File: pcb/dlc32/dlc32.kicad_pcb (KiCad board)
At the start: 2 copper layers, 99.8 x 60.2 mm, 58 parts, among them IC1 74HCT08, IC2 74HCT04, J1 DOOR1, J10 VALVE/CHILLER SSR PWR, J11 Conn_01x02, J12 Conn_01x03, J13 Conn_01x03, J14 Conn_02x05_Odd_Even, J15 Conn_01x05, J16 Conn_01x03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

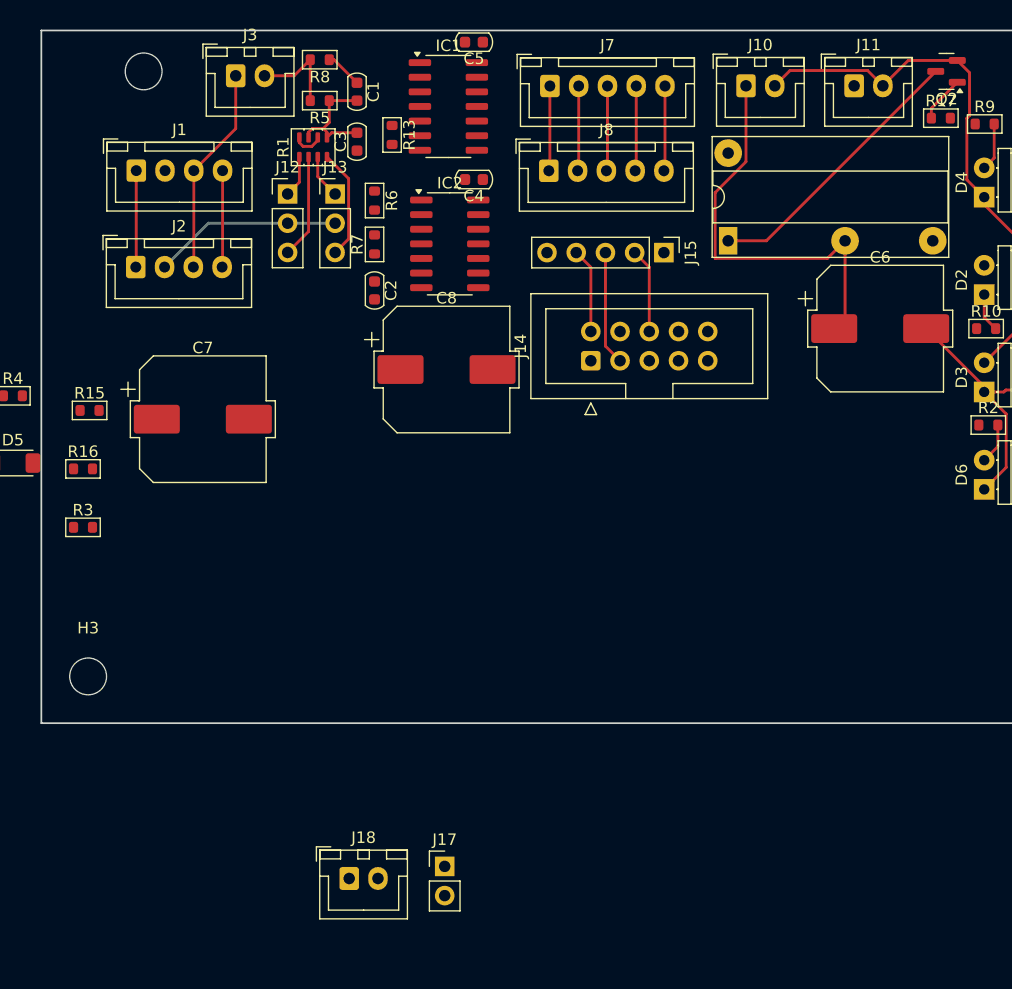
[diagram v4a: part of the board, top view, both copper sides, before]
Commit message: Fix footprint for R1.
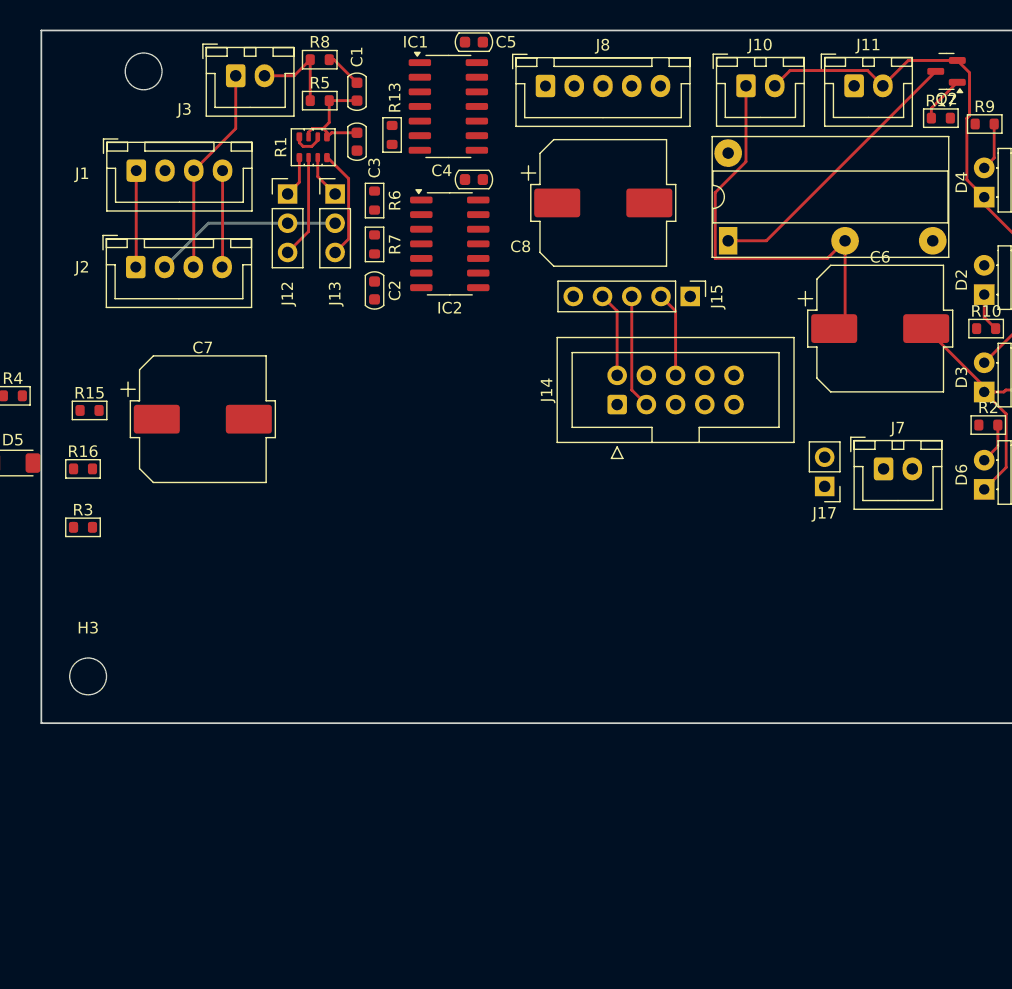
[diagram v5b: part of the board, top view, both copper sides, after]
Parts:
- removed the J7 at (118.1, 29.2)
- J11: value Conn_01x02 -> EXHAUST
- J12: value Conn_01x03 -> DOORJMP1
- J13: value Conn_01x03 -> DOORJMP2
- J14: value Conn_02x05_Odd_Even -> EXT1
- J15: value Conn_01x05 -> COM2
- J16: value Conn_01x03 -> DLC32:J18
- J17: value Conn_01x02 -> EXT PWR
- J7: renamed from J18; value Conn_01x02 -> 5V PWR
- R1: footprint PCM_Resistor_SMD_AKL:R_Array_Concave_4x0603 -> PCM_Resistor_SMD_AKL:R_Array_Convex_4x0603
- moved J7 58.5 mm to (147.1, 62.5)
- moved J17 46.7 mm to (142.0, 64.0), turned to 180 degrees
- moved C8 19.9 mm to (122.7, 39.4)
- moved J8 7.37 mm to (117.7, 29.2)
- moved J14 4.44 mm to (124.0, 56.9)
- moved J15 4.44 mm to (130.3, 47.5)
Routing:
- net GND: track 105.5 -> 98.1 mm
- net +5V: track 28.2 -> 20.8 mm
- net Net-(J8-Pin_4): track 7.40 -> 0.00 mm
- net Net-(J8-Pin_3): track 7.40 -> 0.00 mm
- net Net-(J8-Pin_2): track 7.40 -> 0.00 mm

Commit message: Route some more.
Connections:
- IC1 pad 1: LASER_EN -> Net-(C1-Pad1)
- IC1 pad 11: Net-(IC1-Pad11) -> Net-(J8-Pin_3)
- IC1 pad 12: Net-(C1-Pad1) -> LASER_EN
- IC1 pad 2: Net-(IC1-Pad11) -> Net-(IC1-Pad2)
- IC1 pad 3: Net-(J8-Pin_3) -> Net-(IC1-Pad13)
- IC1 pad 4: Net-(IC1-Pad11) -> Net-(IC1-Pad13)
- IC1 pad 8: Net-(IC1-Pad13) -> Net-(IC1-Pad2)
- IC2 pad 13: Net-(IC1-Pad13) -> Net-(IC1-Pad2)
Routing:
- net +5V: track 20.8 -> 145.2 mm, vias 0 -> 4
- net Net-(J3-Pin_2): track 8.11 -> 93.8 mm
- net Net-(J8-Pin_3): track 0.00 -> 50.7 mm, vias 0 -> 2
- net Net-(IC2-Pad12): track 0.00 -> 47.8 mm, vias 0 -> 2
- net Net-(IC2-Pad10): track 0.00 -> 46.1 mm, vias 0 -> 2
- net GND: track 98.1 -> 141.4 mm
- net FAN: track 0.00 -> 34.5 mm, vias 0 -> 2
- net Net-(J8-Pin_4): track 0.00 -> 20.3 mm, vias 0 -> 1
- net Net-(J1-Pin_2): track 0.00 -> 19.6 mm, vias 0 -> 1
- net Net-(C2-Pad1): track 0.00 -> 19.1 mm, vias 0 -> 2
- net Net-(IC1-Pad2): track 0.00 -> 17.5 mm, vias 0 -> 4
- net Net-(J11-Pin_1): track 0.00 -> 16.3 mm
- net Net-(C3-Pad1): track 0.00 -> 16.0 mm, vias 0 -> 2
- net Net-(IC1-Pad13): track 0.00 -> 6.75 mm
- net Net-(C1-Pad1): track 3.24 -> 9.43 mm
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
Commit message: Route.
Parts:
- added H5: MountingHole, MountingHole:MountingHole_3.2mm_M3, F.Cu at (169.6, 33.2)
- added H6: MountingHole, MountingHole:MountingHole_3.2mm_M3, F.Cu at (169.7, 58.7)
- moved R12 117.5 mm to (109.0, 53.1), turned to 180 degrees
- moved R11 114.2 mm to (109.0, 55.1), turned to 0 degrees
- moved D1 113.4 mm to (111.8, 57.9), turned to 180 degrees
- moved J6 106.4 mm to (113.3, 64.8), turned to 180 degrees
- moved Q1 106.2 mm to (102.5, 55.1), turned to 0 degrees
- moved J4 93.2 mm to (103.6, 64.8), turned to 180 degrees
- moved J5 83.0 mm to (94.5, 64.8), turned to 180 degrees
- moved J9 55.2 mm to (134.4, 62.7)
- moved H4 45.1 mm to (127.5, 64.5)
- moved R4 23.1 mm to (93.9, 50.8), turned to 90 degrees
- moved D5 22.4 mm to (91.4, 51.8), turned to 90 degrees
- moved R3 18.7 mm to (88.4, 52.3), turned to 180 degrees
- moved H3 16.0 mm to (77.5, 64.5)
- moved R16 13.4 mm to (88.9, 55.4), turned to 180 degrees
- moved R15 12.4 mm to (88.4, 50.5)
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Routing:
- net GND: track 141.4 -> 281.0 mm, vias 0 -> 5
- net +V_VALVE: track 44.4 -> 122.7 mm, vias 0 -> 2
- net Net-(D1-A): track 0.00 -> 67.1 mm, vias 0 -> 2
- net LASER_EN: track 0.00 -> 38.2 mm, vias 0 -> 3
- net VALVE_CTRL: track 0.00 -> 33.4 mm
- net Net-(J8-Pin_2): track 0.00 -> 26.9 mm
- net Net-(IC2-Pad9): track 0.00 -> 26.4 mm, vias 0 -> 2
- net FAN: track 34.5 -> 60.2 mm, vias 2 -> 3
- net Net-(D5-K): track 0.00 -> 23.9 mm, vias 0 -> 2
- net Net-(J14-Pin_1): track 0.00 -> 20.3 mm
- net Net-(IC2-Pad6): track 0.00 -> 14.9 mm
- net Net-(J8-Pin_3): track 50.7 -> 62.4 mm
- net Net-(Q1-G): track 0.00 -> 11.0 mm
- net +5V: track 145.2 -> 153.4 mm
- net Net-(J4-Pin_2): track 0.00 -> 6.64 mm
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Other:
- board size 99.8 x 60.2 mm -> 99.8 x 43.9 mm

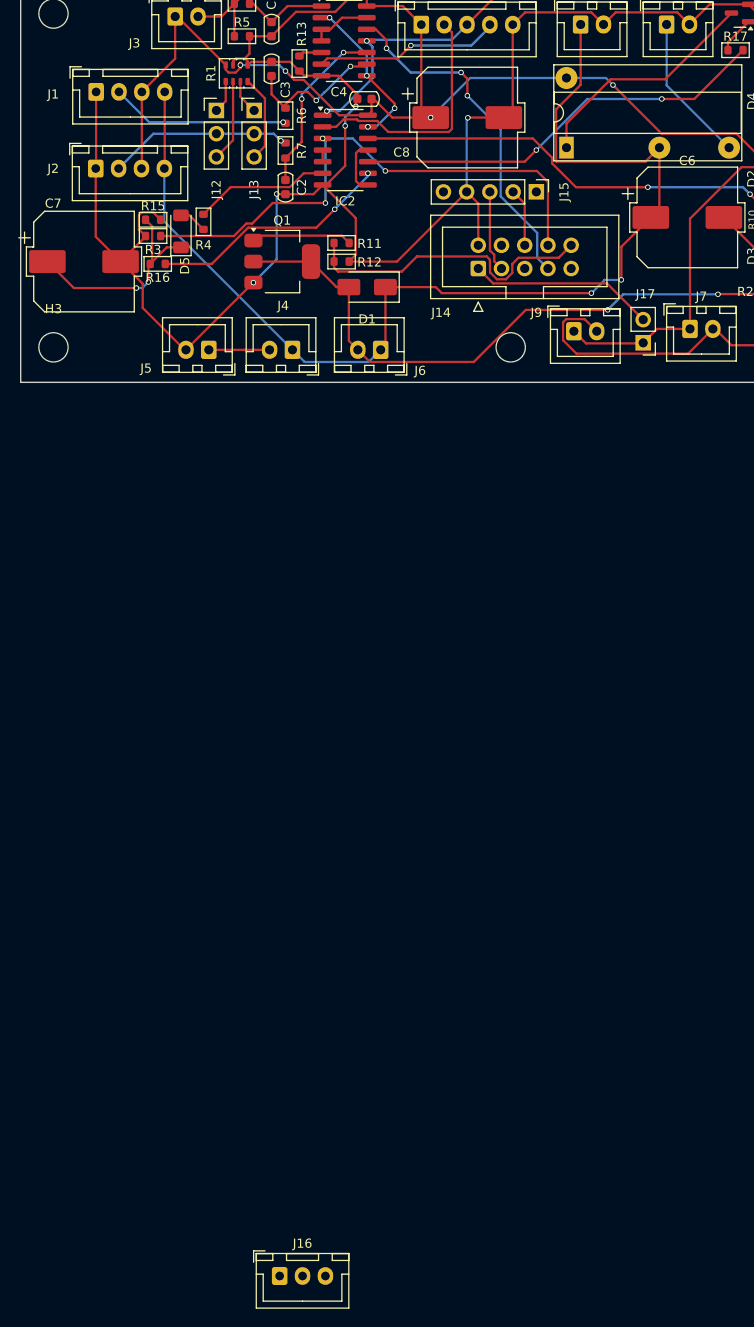
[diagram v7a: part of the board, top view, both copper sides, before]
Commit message: Complete routing.
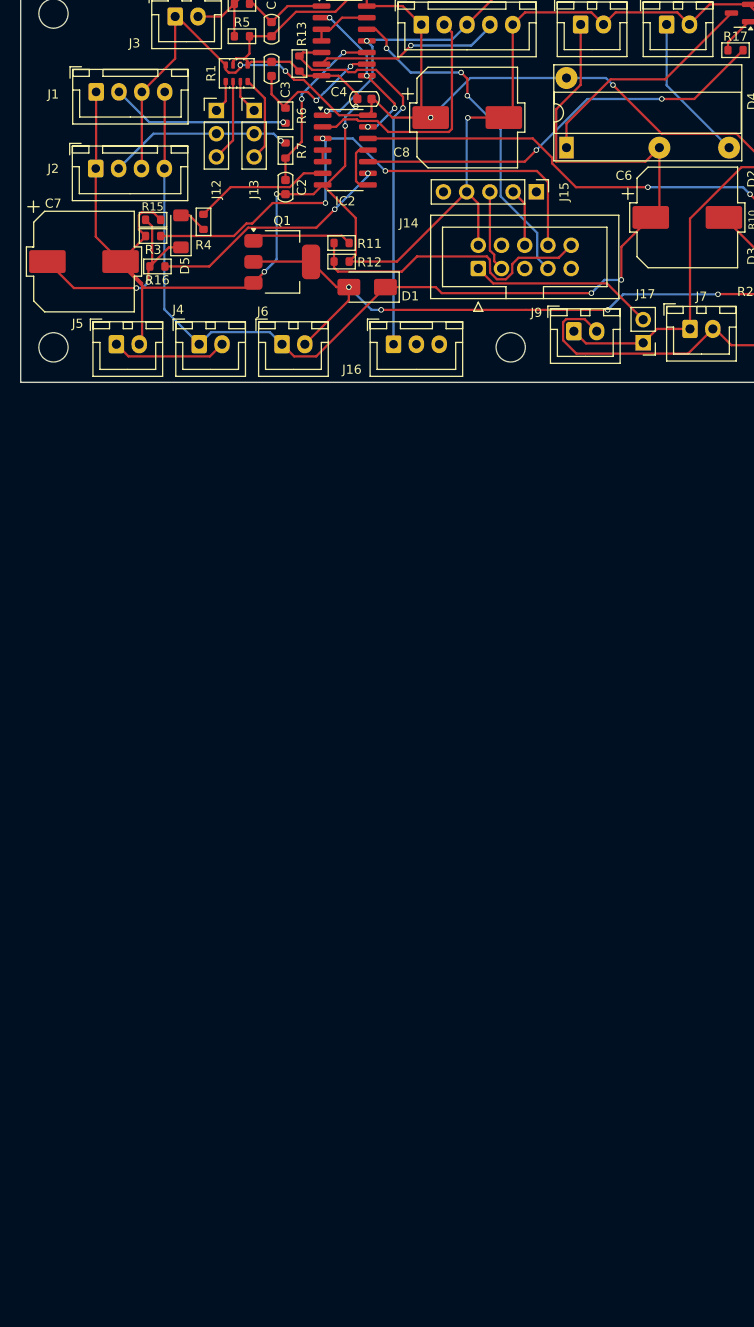
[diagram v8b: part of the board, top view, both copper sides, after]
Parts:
- moved J16 102.6 mm to (114.7, 64.2)
- moved J6 10.8 mm to (102.5, 64.2), turned to 0 degrees
- moved J4 10.2 mm to (93.4, 64.2), turned to 0 degrees
- moved J5 10.1 mm to (84.4, 64.2), turned to 0 degrees
- moved R16 0.28 mm to (88.9, 55.7)
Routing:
- net LASER_PWM: track 2.57 -> 43.5 mm, vias 0 -> 1
- net Net-(J4-Pin_2): track 6.64 -> 12.7 mm
- net GND: track 281.0 -> 284.1 mm
- net +V_VALVE: track 122.7 -> 125.2 mm
- net Net-(D1-A): track 67.1 -> 67.2 mm, vias 2 -> 4
